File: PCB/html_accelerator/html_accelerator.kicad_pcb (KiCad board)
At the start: 4 copper layers, 96.3 x 104.4 mm, 155 parts, among them J1 Bus_PCI_Express_x8, J2 PCIexpress_bracket, U1 MCS9990, U10 AU6438BS, U11 EMMC_4G, U2 AP1513, U3 CAT24C256YI-GT3, U4 AU6438BS, U5 EMMC_4G, U6 EMMC_4G, U7 EMMC_4G, U8 AU6438BS, U9 AU6438BS, Y1 12MHz, Y2 12MHz, Y3 12MHz, Y4 12MHz, Y5 12MHz

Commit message: placement updates
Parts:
- added C68: 0.1uF, Capacitor_SMD:C_0805_2012Metric_Pad1.18x1.45mm_HandSolder, F.Cu at (225.9, 133.8)
- added C69: 0.1uF, Capacitor_SMD:C_0805_2012Metric_Pad1.18x1.45mm_HandSolder, F.Cu at (229.0, 133.8)
- added C70: 0.1uF, Capacitor_SMD:C_0805_2012Metric_Pad1.18x1.45mm_HandSolder, F.Cu at (232.2, 133.8)
- added C71: 100uF, Capacitor_SMD:CP_Elec_6.3x5.8, F.Cu at (156.6, 66.5)
- added C72: 100uF, Capacitor_SMD:CP_Elec_6.3x5.8, F.Cu at (227.7, 142.1)
- added R58: 1k, Resistor_SMD:R_0805_2012Metric_Pad1.20x1.40mm_HandSolder, F.Cu at (220.1, 139.5)
- added R59: 1k, Resistor_SMD:R_0805_2012Metric_Pad1.20x1.40mm_HandSolder, F.Cu at (220.1, 145.2)
- added RN10: 1k, Resistor_SMD:R_Array_Convex_4x1206, F.Cu at (206.1, 142.1)
- added RN12: 1k, Resistor_SMD:R_Array_Convex_4x1206, F.Cu at (213.1, 142.1)
- added RN6: 1k, Resistor_SMD:R_Array_Convex_4x1206, F.Cu at (238.5, 117.3)
- added RN7: 1k, Resistor_SMD:R_Array_Convex_4x1206, F.Cu at (238.5, 124.3)
- added RN8: 1k, Resistor_SMD:R_Array_Convex_4x1206, F.Cu at (238.5, 131.3)
- added U12: MCS9990, Package_QFP:LQFP-128_14x14mm_P0.4mm, F.Cu at (223.9, 121.1)
- C33, C34: value 470uF -> 100uF; footprint Capacitor_SMD:C_0805_2012Metric_Pad1.18x1.45mm_HandSolder -> Capacitor_SMD:CP_Elec_6.3x5.8
- C67: footprint Capacitor_SMD:C_0805_2012Metric_Pad1.18x1.45mm_HandSolder -> Capacitor_SMD:CP_Elec_6.3x5.8
- J1: value Bus_PCI_Express_x8 -> Bus_PCI_Express_x16; footprint Connector_PCBEdge:BUS_PCIexpress_x8 -> Connector_PCBEdge:BUS_PCIexpress_x16
- Y2, Y3, Y4, Y5: footprint Crystal:Crystal_SMD_HC49-SD -> Crystal:Crystal_SMD_3225-4Pin_3.2x2.5mm
- moved RN1 200.3 mm to (210.0, 131.3), turned to 180 degrees
- moved R22 198.1 mm to (196.0, 144.0), turned to 180 degrees
- moved C33 195.0 mm to (237.3, 142.1), turned to 90 degrees
- moved RN2 193.1 mm to (210.0, 124.3), turned to 180 degrees
- moved R33 191.4 mm to (204.2, 133.2)
- moved R29 188.1 mm to (204.2, 111.6)
- moved R36 187.2 mm to (204.2, 130.0)
- moved R34 187.0 mm to (204.2, 123.6)
- moved RN3 186.1 mm to (210.0, 117.3), turned to 180 degrees
- moved R37 185.7 mm to (204.2, 126.8)
- moved R35 185.2 mm to (204.2, 120.5)
- moved R18 183.3 mm to (238.5, 103.3), turned to 180 degrees
- moved R20 182.8 mm to (238.5, 107.1), turned to 180 degrees
- moved C32 180.4 mm to (238.5, 99.5)
- moved R21 177.8 mm to (234.1, 107.1)
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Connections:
- C10 pad 1: +3V3 -> Net-(C10-Pad1)
- C11 pad 1: +3V3 -> Net-(C10-Pad1)
- C12 pad 1: +3V3 -> Net-(C10-Pad1)
- C14 pad 1: +3V3 -> 3v3_filt
- C15 pad 1: +3V3 -> 3v3_filt
- C16 pad 1: +3V3 -> 3v3_filt
- C17 pad 1: +3V3 -> 3v3_filt
- C18 pad 1: +3V3 -> 3v3_filt
- C19 pad 1: +3V3 -> 3v3_filt
- C20 pad 1: +3V3 -> +1V2
- C21 pad 1: +3V3 -> Net-(U1A-+1.2VA_AUX)
- C22 pad 1: +3V3 -> Net-(U1A-+1.2VA_AUX)
- C23 pad 1: +3V3 -> GND
- C24 pad 1: +3V3 -> GND
- C26 pad 1: +3V3 -> Net-(U1A-+3.3VA_AUX)
- C27 pad 1: +3V3 -> Net-(U1A-+3.3VA_AUX)
- C28 pad 1: +3V3 -> Net-(U1A-+3.3VA_AUX)
- C29 pad 1: +3V3 -> Net-(U1A-+3.3VA_AUX)
- C30 pad 1: +3V3 -> Net-(U1A-+3.3VA_AUX)
- C31 pad 1: +3V3 -> GND
- C34 pad 1: +3V3 -> +5V
- C35 pad 2: +3V3 -> 3v3_filt
- C6 pad 1: +3V3 -> +1V2
- C7 pad 1: +3V3 -> Net-(C10-Pad1)
- C8 pad 1: +3V3 -> Net-(C10-Pad1)
- C9 pad 1: +3V3 -> Net-(C10-Pad1)
- FB1 pad 1: +3V3 -> Net-(C10-Pad1)
- FB1 pad 2: +3V3 -> +1V2
- FB2 pad 1: +3V3 -> 3v3_filt
- FB3 pad 1: +3V3 -> Net-(U1A-+1.2VA_AUX)
- FB3 pad 2: +3V3 -> +1V2
- FB4 pad 1: +3V3 -> Net-(U1A-+3.3VA_AUX)
- J1 pad B10: +3V3 -> +3V0
- L1 pad 2: +3V3 -> +5V
- R1 pad 2: +3V3 -> +3V0
- R10 pad 1: +3V3 -> +5V
- R11 pad 1: +3V3 -> +5V
- R12 pad 1: +3V3 -> +5V
- R13 pad 1: +3V3 -> +5V
- R19 pad 1: +3V3 -> +5V
- R22 pad 1: +3V3 -> 3v3_filt
- R23 pad 1: +3V3 -> 3v3_filt
- R24 pad 1: +3V3 -> 3v3_filt
- R25 pad 1: +3V3 -> 3v3_filt
- R26 pad 1: +3V3 -> 3v3_filt
- R27 pad 1: +3V3 -> +3V0
- R28 pad 1: +3V3 -> 3v3_filt
- R42 pad 1: +3V3 -> +5V
- R46 pad 1: +3V3 -> +5V
- R50 pad 1: +3V3 -> +5V
- R54 pad 1: +3V3 -> +5V
- R9 pad 1: +3V3 -> +1V2
- U1 pad 106: +3V3 -> 3v3_filt
- U1 pad 109: +3V3 -> Net-(C10-Pad1)
- U1 pad 110: +3V3 -> Net-(U1A-+3.3VA_AUX)
- U1 pad 111: +3V3 -> Net-(U1A-+3.3VA_AUX)
- U1 pad 119: +3V3 -> Net-(U1A-+3.3VA_AUX)
- U1 pad 12: +3V3 -> Net-(U1A-+1.2VA_AUX)
- U1 pad 121: +3V3 -> Net-(C10-Pad1)
- U1 pad 127: +3V3 -> 3v3_filt
- U1 pad 15: +3V3 -> Net-(U1A-+1.2VA_AUX)
- U1 pad 16: +3V3 -> Net-(U1A-+3.3VA_AUX)
- U1 pad 19: +3V3 -> Net-(U1A-+3.3VA_AUX)
- U1 pad 2: GND -> +3V3
- U1 pad 20: +3V3 -> Net-(C10-Pad1)
- U1 pad 25: +3V3 -> 3v3_filt
- U1 pad 33: +3V3 -> Net-(C10-Pad1)
- U1 pad 48: +3V3 -> 3v3_filt
- U1 pad 51: +3V3 -> Net-(U1A-+3.3VA_AUX)
- U1 pad 52: +3V3 -> Net-(U1A-+3.3VA_AUX)
- U1 pad 58: +3V3 -> Net-(C10-Pad1)
- U1 pad 6: +3V3 -> Net-(U1A-+1.2VA_AUX)
- U1 pad 70: +3V3 -> 3v3_filt
- U1 pad 80: +3V3 -> Net-(C10-Pad1)
- U1 pad 83: +3V3 -> Net-(U1A-+3.3VA_AUX)
- U1 pad 84: +3V3 -> Net-(U1A-+3.3VA_AUX)
- U1 pad 90: +3V3 -> Net-(U1A-+3.3VA_AUX)
- U1 pad 91: +3V3 -> Net-(U1A-+3.3VA_AUX)
- U1 pad 98: +3V3 -> Net-(C10-Pad1)
- U10 pad 15: +3V3 -> +5V
- U3 pad 5: Net-(U1E-EE_SDA) -> Net-(U1E-EE_SCL)
- U3 pad 6: Net-(U1E-EE_SCL) -> Net-(U1E-EE_SDA)
- U3 pad 8: +3V3 -> 3v3_filt
- U4 pad 15: +3V3 -> +5V
- U8 pad 15: +3V3 -> +5V
- U9 pad 15: +3V3 -> +5V
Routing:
- net unconnected-(J1-PETn6-PadB42): track 10.3 -> 0.00 mm
- net unconnected-(J1-PETn4-PadB34): track 10.3 -> 0.00 mm
- net unconnected-(J1-PETn2-PadB24): track 10.3 -> 0.00 mm
- net unconnected-(J1-PETp6-PadB41): track 10.3 -> 0.00 mm
- net unconnected-(J1-PETp4-PadB33): track 10.3 -> 0.00 mm
- net unconnected-(J1-PETp2-PadB23): track 10.3 -> 0.00 mm
- net unconnected-(J1-PETn7-PadB46): track 7.09 -> 0.00 mm
- net unconnected-(J1-PETn5-PadB38): track 7.09 -> 0.00 mm
- net unconnected-(J1-PETn1-PadB20): track 7.09 -> 0.00 mm
- net unconnected-(J1-PETn3-PadB28): track 7.09 -> 0.00 mm
- net unconnected-(J1-PETp7-PadB45): track 7.09 -> 0.00 mm
- net unconnected-(J1-PETp3-PadB27): track 7.09 -> 0.00 mm
- net unconnected-(J1-PETp1-PadB19): track 7.09 -> 0.00 mm
- net unconnected-(J1-PETp5-PadB37): track 7.09 -> 0.00 mm
- net unconnected-(J1-PERn7-PadA48): track 7.06 -> 0.00 mm
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- added copper zone on B.Cu, net GND
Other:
- board size 96.3 x 104.4 mm -> 129.3 x 104.4 mm

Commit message: layout and 3d updates
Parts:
- removed C66: 0.1uF, Capacitor_SMD:C_0805_2012Metric_Pad1.18x1.45mm_HandSolder
- removed C67: 470uF, Capacitor_SMD:CP_Elec_6.3x5.8
- removed R66: 3k, Resistor_SMD:R_0805_2012Metric_Pad1.20x1.40mm_HandSolder
- added D3: RED, LED_SMD:LED_0805_2012Metric_Pad1.15x1.40mm_HandSolder, F.Cu at (138.2, 114.8)
- added D4: RED, LED_SMD:LED_0805_2012Metric_Pad1.15x1.40mm_HandSolder, F.Cu at (138.2, 133.8)
- added D5: RED, LED_SMD:LED_0805_2012Metric_Pad1.15x1.40mm_HandSolder, F.Cu at (138.2, 76.7)
- added MECH1: ~, html_accel_footprints:Heatsink, F.Cu at (198.5, 51.6)
- added MECH2: ~, html_accel_footprints:Heatsink, F.Cu at (158.6, 51.6)
- moved D2 53.7 mm to (138.2, 95.7), turned to 180 degrees
- moved R47 8.26 mm to (150.3, 116.0), turned to -90 degrees
- moved R43 8.25 mm to (150.3, 97.0), turned to -90 degrees
- moved R51 8.25 mm to (150.3, 135.1), turned to -90 degrees
- moved R55 8.25 mm to (150.3, 77.9), turned to -90 degrees
- moved C34 3.81 mm to (152.8, 57.0)
- moved C71 3.81 mm to (152.8, 66.5)
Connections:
- net /PCIE_Slot/PCIE_RXn renamed /PCIE_Slot/50_PCIE_RX_N
- net /PCIE_Slot/PCIE_RXp renamed /PCIE_Slot/50_PCIE_RX_P
- net /PCIE_Slot/PCIE_TXn renamed /PCIE_Slot/50_PCIE_TX_N
- net /PCIE_Slot/PCIE_TXp renamed /PCIE_Slot/50_PCIE_TX_P
- net Net-(J1-REFCLK+) renamed /PCIE_Slot/50_PCIE_CLK_P
- net Net-(J1-REFCLK-) renamed /PCIE_Slot/50_PCIE_CLK_N
- net Net-(U10-DATA0) renamed /eMMC4/DATA_0
- net Net-(U10-DATA1) renamed /eMMC4/DATA_1
- net Net-(U10-DATA2) renamed /eMMC4/DATA_2
- net Net-(U10-DATA3) renamed /eMMC4/DATA_3
- net Net-(U10-DATA4) renamed /eMMC4/DATA_4
- net Net-(U10-DATA5) renamed /eMMC4/DATA_5
- net Net-(U10-DATA6) renamed /eMMC4/DATA_6
- net Net-(U10-DATA7) renamed /eMMC4/DATA_7
- net Net-(U1C-PCIE_TXDN) renamed /PCIE_Slot/50_PCIE_TXC_N
- net Net-(U1C-PCIE_TXDP) renamed /PCIE_Slot/50_PCIE_TXC_P
- net Net-(U4-DATA0) renamed /eMMC1/DATA_0
- net Net-(U4-DATA1) renamed /eMMC1/DATA_1
- net Net-(U4-DATA2) renamed /eMMC1/DATA_2
- net Net-(U4-DATA3) renamed /eMMC1/DATA_3
- net Net-(U4-DATA4) renamed /eMMC1/DATA_4
- net Net-(U4-DATA5) renamed /eMMC1/DATA_5
- net Net-(U4-DATA6) renamed /eMMC1/DATA_6
- net Net-(U4-DATA7) renamed /eMMC1/DATA_7
- net Net-(U6A-DAT0) renamed /eMMC2/DATA_0
- net Net-(U6A-DAT1) renamed /eMMC2/DATA_1
- net Net-(U6A-DAT2) renamed /eMMC2/DATA_2
- net Net-(U6A-DAT3) renamed /eMMC2/DATA_3
- net Net-(U6A-DAT4) renamed /eMMC2/DATA_4
- net Net-(U6A-DAT5) renamed /eMMC2/DATA_5
- net Net-(U6A-DAT6) renamed /eMMC2/DATA_6
- net Net-(U6A-DAT7) renamed /eMMC2/DATA_7
- net Net-(U7A-DAT0) renamed /eMMC3/DATA_0
- net Net-(U7A-DAT1) renamed /eMMC3/DATA_1
- net Net-(U7A-DAT2) renamed /eMMC3/DATA_2
- net Net-(U7A-DAT3) renamed /eMMC3/DATA_3
- net Net-(U7A-DAT4) renamed /eMMC3/DATA_4
- net Net-(U7A-DAT5) renamed /eMMC3/DATA_5
- net Net-(U7A-DAT6) renamed /eMMC3/DATA_6
- net Net-(U7A-DAT7) renamed /eMMC3/DATA_7
- D2 pad 1: unconnected-(D2-K-Pad1) -> USB0_LED
- D2 pad 2: unconnected-(D2-A-Pad2) -> +5V
- U1 pad 112: USB2_DM -> 90_USB2_D_N
- U1 pad 113: USB2_DP -> 90_USB2_D_P
- U1 pad 53: USB3_DM -> 90_USB3_D_N
- U1 pad 54: USB3_DP -> 90_USB3_D_P
- U1 pad 85: USB0_DM -> 90_USB0_D_N
- U1 pad 86: USB0_DP -> 90_USB0_D_P
- U1 pad 92: USB1_DM -> 90_USB1_D_N
- U1 pad 93: USB1_DP -> 90_USB1_D_P
- U10 pad 7: USB3_DM -> 90_USB3_D_P
- U10 pad 8: USB3_DP -> 90_USB3_D_N
- U12 pad 1: unconnected-(U12A-GND1-Pad1) -> GND
- U12 pad 10: unconnected-(U12C-PCIE_RXDP-Pad10) -> GND
- U12 pad 100: unconnected-(U12D-USB0_PWR_EN_N-Pad100) -> GND
- U12 pad 101: unconnected-(U12E-LN_STAT2-Pad101) -> GND
- U12 pad 102: unconnected-(U12D-USB1_OVCI_N-Pad102) -> GND
- U12 pad 103: unconnected-(U12D-USB1_PWR_EN_N-Pad103) -> GND
- U12 pad 104: unconnected-(U12E-LN_STAT0-Pad104) -> GND
- U12 pad 105: unconnected-(U12E-LN_STAT1-Pad105) -> GND
- U12 pad 106: unconnected-(U12A-+3.3VIO-Pad106) -> GND
- U12 pad 107: unconnected-(U12A-GND20-Pad107) -> GND
- U12 pad 108: unconnected-(U12A-GND21-Pad108) -> GND
- U12 pad 109: unconnected-(U12A-+1.2V-Pad109) -> GND
- U12 pad 11: unconnected-(U12A-GND3-Pad11) -> GND
- U12 pad 110: unconnected-(U12A-+3.3VA-Pad110) -> GND
- U12 pad 111: unconnected-(U12A-+3.3VA-Pad111) -> GND
- U12 pad 112: unconnected-(U12D-USB2_DM-Pad112) -> GND
- U12 pad 113: unconnected-(U12D-USB2_DP-Pad113) -> GND
- U12 pad 114: unconnected-(U12A-GND22-Pad114) -> GND
- U12 pad 115: unconnected-(U12A-GND23-Pad115) -> GND
- U12 pad 116: unconnected-(U12D-USB2_IBERF-Pad116) -> GND
- U12 pad 117: unconnected-(U12D-USB2_OTG_VBUS-Pad117) -> GND
- U12 pad 118: unconnected-(U12A-GND24-Pad118) -> GND
- U12 pad 119: unconnected-(U12A-+3.3VA-Pad119) -> GND
- U12 pad 12: unconnected-(U12A-+1.2VA-Pad12) -> GND
- U12 pad 120: unconnected-(U12A-GND25-Pad120) -> GND
- U12 pad 121: unconnected-(U12A-+1.2V-Pad121) -> GND
- U12 pad 122: unconnected-(U12D-USB2_OVCI_N-Pad122) -> GND
- U12 pad 123: unconnected-(U12D-USB2_PWR_EN_N-Pad123) -> GND
- U12 pad 124: unconnected-(U12D-USB2_OTG_ID-Pad124) -> GND
- U12 pad 125: unconnected-(U12D-USB3_OVCI_N-Pad125) -> GND
- U12 pad 126: unconnected-(U12D-USB3_PWR_EN_N-Pad126) -> GND
- U12 pad 127: unconnected-(U12A-+3.3VIO-Pad127) -> GND
- U12 pad 128: unconnected-(U12A-GND26-Pad128) -> GND
- U12 pad 13: unconnected-(U12C-PCIE_TXDP-Pad13) -> GND
- U12 pad 14: unconnected-(U12C-PCIE_TXDN-Pad14) -> GND
- U12 pad 15: unconnected-(U12A-+1.2VA-Pad15) -> GND
- U12 pad 16: unconnected-(U12A-+3.3VA_PLL-Pad16) -> GND
- U12 pad 17: unconnected-(U12A-GND4-Pad17) -> GND
- U12 pad 18: unconnected-(U12A-GND5-Pad18) -> GND
- U12 pad 19: unconnected-(U12A-+3.3VA_AUX-Pad19) -> GND
- U12 pad 2: unconnected-(U12A-+3.3VIN_REG-Pad2) -> GND
- U12 pad 20: unconnected-(U12A-+1.2V-Pad20) -> GND
- U12 pad 21: unconnected-(U12A-GND6-Pad21) -> GND
- U12 pad 22: unconnected-(U12C-PCIE_CLKREQ_N-Pad22) -> GND
- U12 pad 23: unconnected-(U12C-PCIE_WAKE_N-Pad23) -> GND
- U12 pad 24: unconnected-(U12E-MODE_SEL0-Pad24) -> GND
- U12 pad 25: unconnected-(U12A-+3.3VIO-Pad25) -> GND
- U12 pad 26: unconnected-(U12A-GND7-Pad26) -> GND
- U12 pad 27: unconnected-(U12E-OTG_EN_N-Pad27) -> GND
- U12 pad 28: unconnected-(U12C-PCIE_PERST_N-Pad28) -> GND
- U12 pad 29: unconnected-(U12E-EE_SCL-Pad29) -> GND
- U12 pad 3: unconnected-(U12A-+1.2VOUT_REG-Pad3) -> GND
- U12 pad 30: unconnected-(U12E-EE_SDA-Pad30) -> GND
- U12 pad 31: unconnected-(U12E-SCAN_EN-Pad31) -> GND
- U12 pad 32: unconnected-(U12E-TEST_EN-Pad32) -> GND
- U12 pad 33: unconnected-(U12A-+1.2V-Pad33) -> GND
- U12 pad 34: unconnected-(U12A-GND8-Pad34) -> GND
- U12 pad 35: unconnected-(U12B-GPIO0/D0-Pad35) -> GND
- U12 pad 36: unconnected-(U12B-GPIO1/D1-Pad36) -> GND
- U12 pad 37: unconnected-(U12B-GPIO2/D2-Pad37) -> GND
- U12 pad 38: unconnected-(U12B-GPIO3/D3-Pad38) -> GND
- U12 pad 39: unconnected-(U12B-GPIO4/D4-Pad39) -> GND
- U12 pad 4: unconnected-(U12C-PCIE_REFCLKN-Pad4) -> GND
- U12 pad 40: unconnected-(U12B-GPIO5/D5-Pad40) -> GND
- U12 pad 41: unconnected-(U12B-GPIO6/D6-Pad41) -> GND
- U12 pad 42: unconnected-(U12B-GPIO7/D7-Pad42) -> GND
- U12 pad 43: unconnected-(U12B-GPIO8/INTA-Pad43) -> GND
- U12 pad 44: unconnected-(U12B-GPIO9/INTB-Pad44) -> GND
- U12 pad 45: unconnected-(U12B-GPIO10/INTC-Pad45) -> GND
- U12 pad 46: unconnected-(U12B-GPIO11/INTD-Pad46) -> GND
- U12 pad 47: unconnected-(U12E-MODE_SEL1-Pad47) -> GND
- U12 pad 48: unconnected-(U12A-+3.3VIO-Pad48) -> GND
- U12 pad 49: unconnected-(U12E-MODE_SEL2-Pad49) -> GND
- U12 pad 5: unconnected-(U12C-PCIE_REFCLKP-Pad5) -> GND
- U12 pad 50: unconnected-(U12A-GND9-Pad50) -> GND
- U12 pad 51: unconnected-(U12A-+3.3VA-Pad51) -> GND
- U12 pad 52: unconnected-(U12A-+3.3VA-Pad52) -> GND
- U12 pad 53: unconnected-(U12D-USB3_DM-Pad53) -> GND
- U12 pad 54: unconnected-(U12D-USB3_DP-Pad54) -> GND
- U12 pad 55: unconnected-(U12A-GND10-Pad55) -> GND
- U12 pad 56: unconnected-(U12A-GND11-Pad56) -> GND
- U12 pad 57: unconnected-(U12D-USB3_IBREF-Pad57) -> GND
- U12 pad 58: unconnected-(U12A-+1.2V-Pad58) -> GND
- U12 pad 59: unconnected-(U12A-GND12-Pad59) -> GND
- U12 pad 6: unconnected-(U12A-+1.2VA_AUX-Pad6) -> GND
- U12 pad 60: unconnected-(U12E-JTAG_TCK-Pad60) -> GND
- U12 pad 61: unconnected-(U12E-JTAG_TDI-Pad61) -> GND
- U12 pad 62: unconnected-(U12E-JTAG_TDO-Pad62) -> GND
- U12 pad 63: unconnected-(U12E-JTAG_TMS-Pad63) -> GND
- U12 pad 64: unconnected-(U12E-JTAG_TRST_N-Pad64) -> GND
- U12 pad 65: unconnected-(U12B-GPIO12/CSA_N-Pad65) -> GND
- U12 pad 66: unconnected-(U12B-GPIO13/CSB_N-Pad66) -> GND
- U12 pad 67: unconnected-(U12B-GPIO14/CSC_N-Pad67) -> GND
- U12 pad 68: unconnected-(U12B-GPIO15/CSD_N-Pad68) -> GND
- U12 pad 69: unconnected-(U12A-GND13-Pad69) -> GND
- U12 pad 7: unconnected-(U12C-REXT-Pad7) -> GND
- U12 pad 70: unconnected-(U12A-+3.3VIO-Pad70) -> GND
- U12 pad 71: unconnected-(U12B-GPIO16/RESET-Pad71) -> GND
- U12 pad 72: unconnected-(U12B-GPIO17/IOW_N-Pad72) -> GND
- U12 pad 73: unconnected-(U12B-GPIO18/IOR_N-Pad73) -> GND
- U12 pad 74: unconnected-(U12B-GPIO23/IOCHRDY2-Pad74) -> GND
- U12 pad 75: unconnected-(U12B-GPIO19/A0-Pad75) -> GND
- U12 pad 76: unconnected-(U12B-GPIO20/A1-Pad76) -> GND
- U12 pad 77: unconnected-(U12B-GPIO21/A2-Pad77) -> GND
- U12 pad 78: unconnected-(U12B-GPIO22/IOCHRDY1-Pad78) -> GND
- U12 pad 79: unconnected-(U12A-GND14-Pad79) -> GND
- U12 pad 8: unconnected-(U12A-GND2-Pad8) -> GND
- U12 pad 80: unconnected-(U12A-+1.2V-Pad80) -> GND
- U12 pad 81: unconnected-(U12B-USB0_XSCI-Pad81) -> GND
- U12 pad 82: unconnected-(U12B-USB0_XSCO-Pad82) -> GND
- U12 pad 83: unconnected-(U12A-+3.3VA-Pad83) -> GND
- U12 pad 84: unconnected-(U12A-+3.3VA-Pad84) -> GND
- U12 pad 85: unconnected-(U12D-USB0_DM-Pad85) -> GND
- U12 pad 86: unconnected-(U12D-USB0_DP-Pad86) -> GND
- U12 pad 87: unconnected-(U12A-GND15-Pad87) -> GND
- U12 pad 88: unconnected-(U12A-GND16-Pad88) -> GND
- U12 pad 89: unconnected-(U12D-USB0_IBREF-Pad89) -> GND
- U12 pad 9: unconnected-(U12C-PCIE_RXDN-Pad9) -> GND
- U12 pad 90: unconnected-(U12A-+3.3VA-Pad90) -> GND
- U12 pad 91: unconnected-(U12A-+3.3VA-Pad91) -> GND
- U12 pad 92: unconnected-(U12D-USB1_DM-Pad92) -> GND
- U12 pad 93: unconnected-(U12D-USB1_DP-Pad93) -> GND
- U12 pad 94: unconnected-(U12A-GND17-Pad94) -> GND
- U12 pad 95: unconnected-(U12A-GND18-Pad95) -> GND
- U12 pad 96: unconnected-(U12D-USB1_IBREF-Pad96) -> GND
- U12 pad 97: unconnected-(U12A-GND19-Pad97) -> GND
- U12 pad 98: unconnected-(U12A-+1.2V-Pad98) -> GND
- U12 pad 99: unconnected-(U12D-USB0_OVCI_N-Pad99) -> GND
- U4 pad 7: USB0_DM -> 90_USB0_D_P
- U4 pad 8: USB0_DP -> 90_USB0_D_N
- U8 pad 7: USB1_DM -> 90_USB1_D_P
- U8 pad 8: USB1_DP -> 90_USB1_D_N
- U9 pad 7: USB2_DM -> 90_USB2_D_P
- U9 pad 8: USB2_DP -> 90_USB2_D_N
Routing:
- net /PCIE_Slot/50_PCIE_CLK_N: track 0.00 -> 3.93 mm
- net /PCIE_Slot/50_PCIE_CLK_P: track 0.00 -> 3.93 mm
- net /PCIE_Slot/50_PCIE_RX_N: track 10.3 -> 9.67 mm
- net /PCIE_Slot/50_PCIE_RX_P: track 10.3 -> 9.69 mm
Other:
- rule pad_to_mask_clearance: 0.051 -> 0.04
- rule solder_mask_min_width: 0.25 -> 0.1

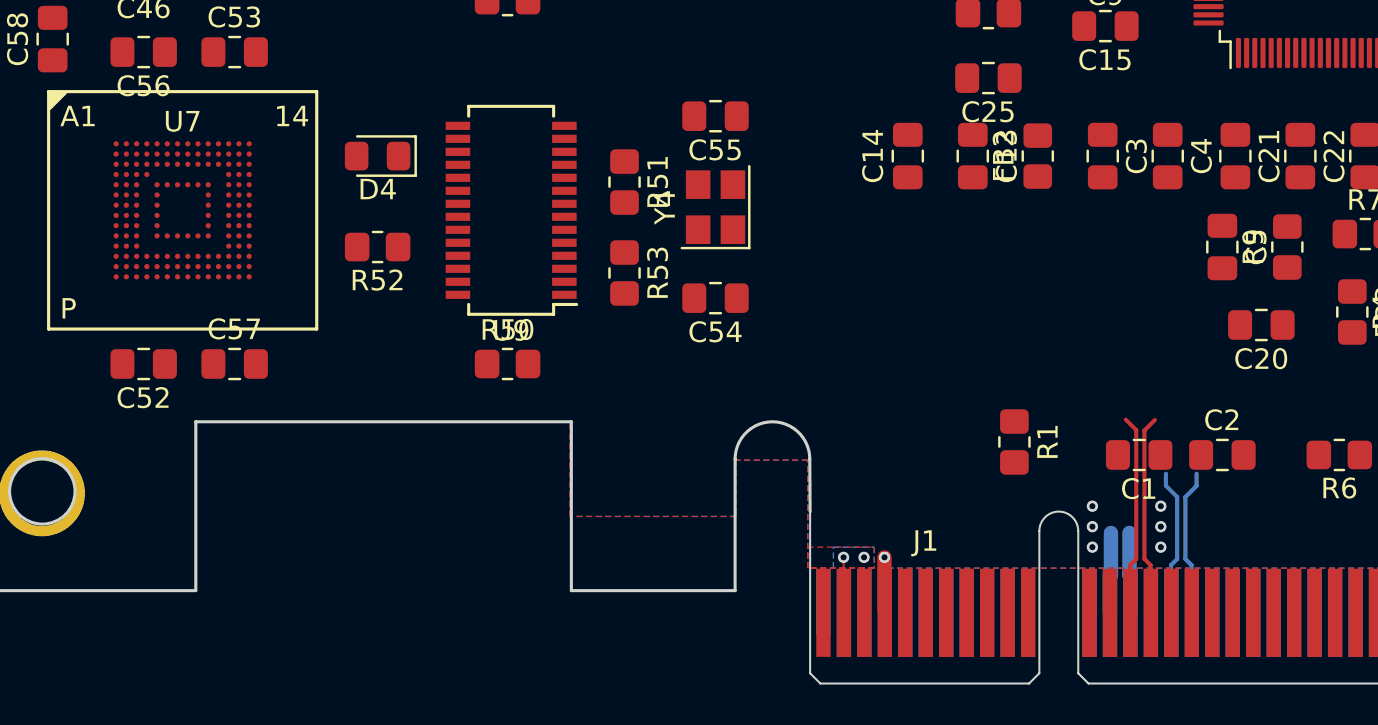
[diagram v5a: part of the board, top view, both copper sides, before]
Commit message: impedance controlled nets
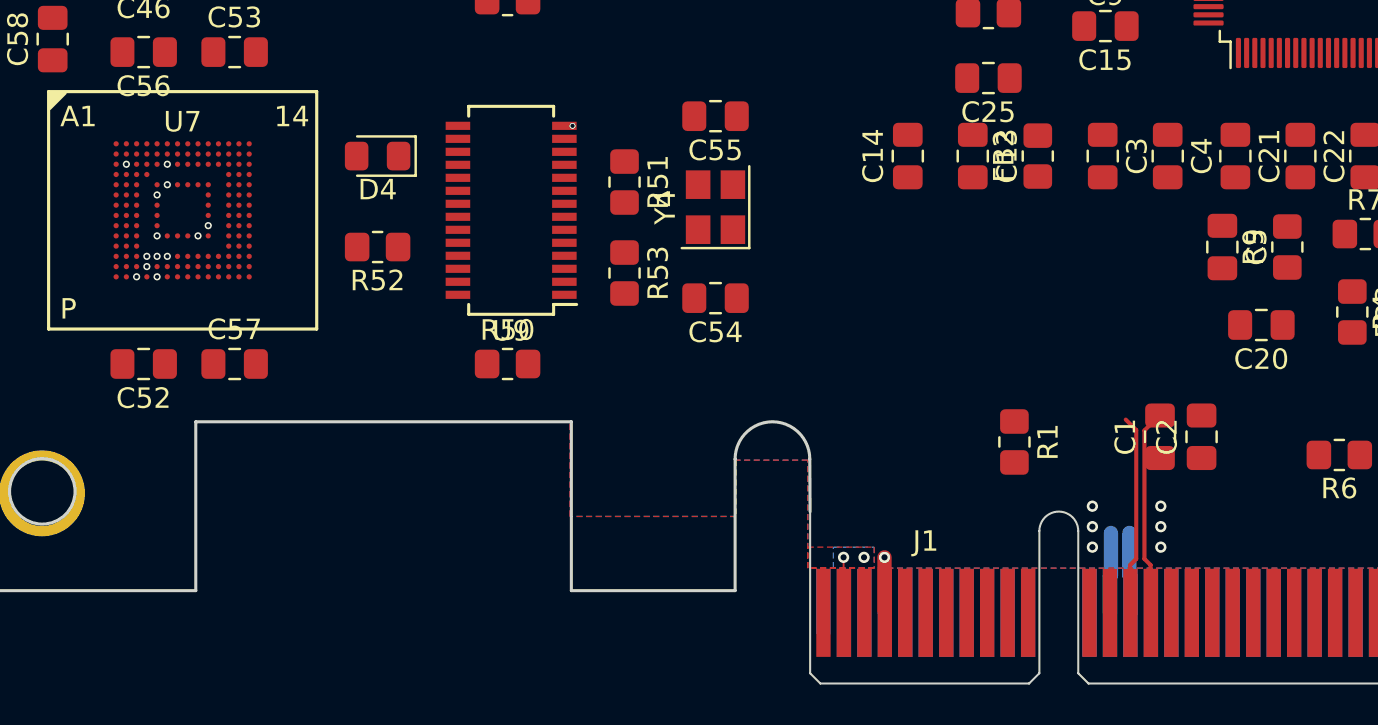
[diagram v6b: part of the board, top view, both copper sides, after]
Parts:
- moved C1 1.35 mm to (176.4, 147.5), turned to 90 degrees
- moved C2 1.35 mm to (178.5, 147.5), turned to 90 degrees
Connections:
- net /PCIE_Slot/50_PCIE_CLK_N renamed /PCIE_Slot/85_PCIE_CLK_N
- net /PCIE_Slot/50_PCIE_CLK_P renamed /PCIE_Slot/85_PCIE_CLK_P
- net /PCIE_Slot/50_PCIE_RX_N renamed /PCIE_Slot/85_PCIE_RX_N
- net /PCIE_Slot/50_PCIE_RX_P renamed /PCIE_Slot/85_PCIE_RX_P
- net /PCIE_Slot/50_PCIE_TXC_N renamed /PCIE_Slot/85_PCIE_TXC_N
- net /PCIE_Slot/50_PCIE_TXC_P renamed /PCIE_Slot/85_PCIE_TXC_P
- net /PCIE_Slot/50_PCIE_TX_N renamed /PCIE_Slot/85_PCIE_TX_N
- net /PCIE_Slot/50_PCIE_TX_P renamed /PCIE_Slot/85_PCIE_TX_P
- net Net-(U10-VDD_FLASH_3.3_OUT) renamed /eMMC4/VDD_3v3_EMMC4
- net Net-(U4-VDD_FLASH_3.3_OUT) renamed /eMMC1/VDD_3v3_EMMC1
- net Net-(U8-VDD_FLASH_3.3_OUT) renamed /eMMC2/VDD_3v3_EMMC2
- net Net-(U9-VDD_FLASH_3.3_OUT) renamed /eMMC3/VDD_3v3_EMMC3
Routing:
- net /eMMC3/VDD_3v3_EMMC3: track 0.00 -> 11.5 mm, vias 0 -> 10
- net /PCIE_Slot/85_PCIE_TX_N: track 7.06 -> 0.00 mm
- net /PCIE_Slot/85_PCIE_TX_P: track 7.06 -> 0.00 mm
- net Net-(U7A-VDDI): vias 0 -> 1
- net Net-(U7A-RST_N): vias 0 -> 1
- net Net-(U7A-CMD): vias 0 -> 1
- net Net-(U7A-CLK): vias 0 -> 1
- added copper zone on In1.Cu, net /eMMC3/VDD_3v3_EMMC3
